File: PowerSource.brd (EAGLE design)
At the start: 95 x 72 mm, 11 parts

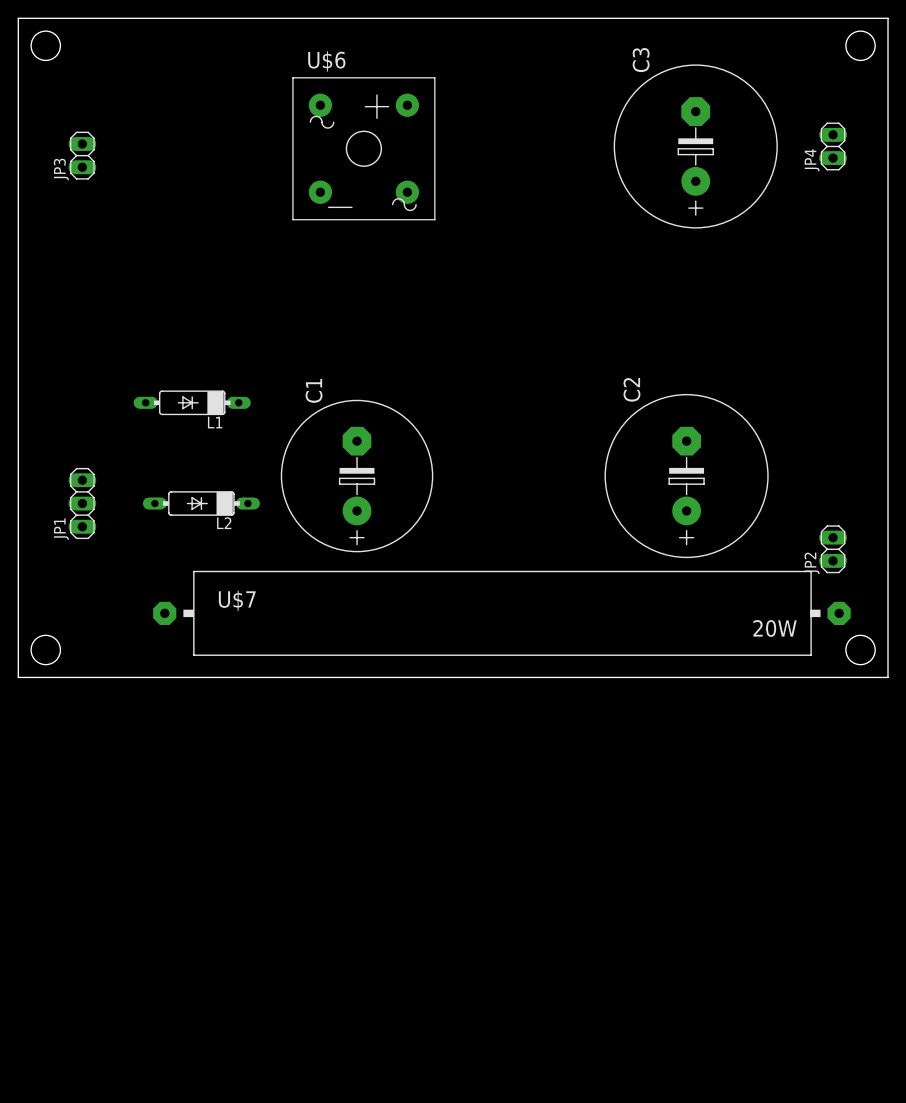
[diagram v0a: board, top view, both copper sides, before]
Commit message: [fix]電源回路を手直し
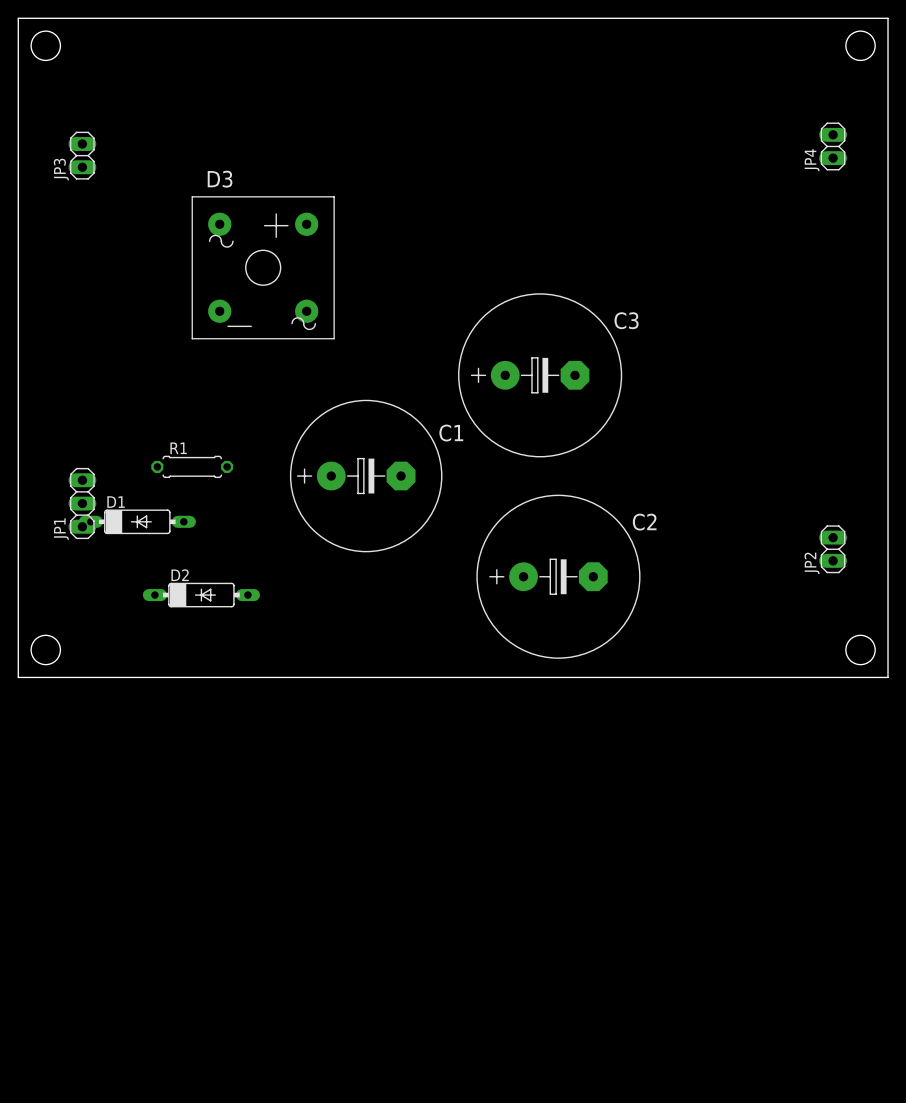
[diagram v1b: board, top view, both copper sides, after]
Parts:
- removed L1, L2: DIODE, VacuumTube:DO07
- removed U$6: BRIDGERECTIFIER, VacuumTube:BRIDGERECTIFIER
- removed U$7: RESISTOR, VacuumTube:RESISTOR
- added D1, D2: (no value), VacuumTube:DO07
- added D3: (no value), VacuumTube:BRIDGERECTIFIER
- added R1: (no value), VacuumTube:0207/7
- C1: value E7.5-16 -> 47u
- C2: value E7.5-18 -> 100u
- C3: value E7.5-18 -> 8800u
- moved C3 30.2 mm to (57.0, 33.0), turned to 0 degrees
- moved C2 17.8 mm to (59.0, 11.0), turned to 0 degrees
- moved C1 1.00 mm to (38.0, 22.0), turned to 0 degrees
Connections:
- net GND: now also D3.AC2; no longer U$6.AC2
- net N$1: now also D2.A; no longer L2.A
- net N$14: now also R1.2; no longer U$7.2
- net N$15: now also D1.C, D2.C, R1.1; no longer L1.C, L2.C, U$7.1
- net N$2: now also D1.A; no longer L1.A
- net N$3: now also D3.-; no longer U$6.-
- net N$4: now also D3.+; no longer U$6.+
- net N$7: now also D3.AC1; no longer U$6.AC1

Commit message: [fix]電源の重大な欠陥
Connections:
- net GND: now also D3.-; no longer D3.AC2
- net N$3: now also D3.AC1; no longer D3.-
- net N$4: now also D3.AC2; no longer D3.+
- net N$7: now also D3.+; no longer D3.AC1
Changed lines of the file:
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@@
 <contactref element="JP2" pad="2"/>
 <contactref element="JP4" pad="2"/>
-<contactref element="D3" pad="AC2"/>
 <contactref element="C1" pad="-"/>
 <contactref element="C2" pad="-"/>
 <contactref element="C3" pad="-"/>
-<wire x1="89" y1="15.27" x2="89" y2="59.27" width="0" layer="19" extent="1-1"/>
-<wire x1="7" y1="16.46" x2="89" y2="15.27" width="0" layer="19" extent="1-1"/>
-<wire x1="31.5" y1="40" x2="7" y2="16.46" width="0" layer="19" extent="1-1"/>
-<wire x1="41.81" y1="22" x2="31.5" y2="40" width="0" layer="19" extent="1-1"/>
-<wire x1="62.81" y1="11" x2="41.81" y2="22" width="0" layer="19" extent="1-1"/>
-<wire x1="60.81" y1="33" x2="62.81" y2="11" width="0" layer="19" extent="1-1"/>
+<contactref element="D3" pad="-"/>
+<wire x1="60.81" y1="33" x2="89" y2="59.27" width="0" layer="19" extent="1-1"/>
+<wire x1="41.81" y1="22" x2="60.81" y2="33" width="0" layer="19" extent="1-1"/>
+<wire x1="62.81" y1="11" x2="60.81" y2="33" width="0" layer="19" extent="1-1"/>
+<wire x1="89" y1="15.27" x2="62.81" y2="11" width="0" layer="19" extent="1-1"/>
+<wire x1="22" y1="40" x2="41.81" y2="22" width="0" layer="19" extent="1-1"/>
+<wire x1="7" y1="16.46" x2="22" y2="40" width="0" layer="19" extent="1-1"/>
 </signal>
 <signal name="N$14">
@@
 <signal name="N$7">
 <contactref element="JP4" pad="1"/>
-<contactref element="D3" pad="AC1"/>
 <contactref element="C3" pad="+"/>
-<wire x1="22" y1="49.5" x2="89" y2="56.73" width="0" layer="19" extent="1-1"/>
-<wire x1="53.19" y1="33" x2="22" y2="49.5" width="0" layer="19" extent="1-1"/>
+<contactref element="D3" pad="+"/>
+<wire x1="53.19" y1="33" x2="89" y2="56.73" width="0" layer="19" extent="1-1"/>
+<wire x1="31.5" y1="49.5" x2="53.19" y2="33" width="0" layer="19" extent="1-1"/>
 </signal>
 <signal name="N$1">
@@
 <wire x1="18.08" y1="17" x2="7" y2="21.54" width="0" layer="19" extent="1-1"/>
 </signal>
-<signal name="N$4">
-<contactref element="JP3" pad="1"/>
-<contactref element="D3" pad="+"/>
-<wire x1="31.5" y1="49.5" x2="7" y2="55.73" width="0" layer="19" extent="1-1"/>
-</signal>
 <signal name="N$3">
 <contactref element="JP3" pad="2"/>
-<contactref element="D3" pad="-"/>
-<wire x1="22" y1="40" x2="7" y2="58.27" width="0" layer="19" extent="1-1"/>
+<contactref element="D3" pad="AC1"/>
+<wire x1="7" y1="58.27" x2="22" y2="49.5" width="0" layer="19" extent="1-1"/>
+</signal>
+<signal name="N$4">
+<contactref element="D3" pad="AC2"/>
+<contactref element="JP3" pad="1"/>
+<wire x1="7" y1="55.73" x2="31.5" y2="40" width="0" layer="19" extent="1-1"/>
 </signal>
 </signals>

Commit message: [fix]電源の直し
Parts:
- C1: value 47u -> 100u
- C2: value 100u -> 47u
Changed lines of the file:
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@@
 <attribute name="VALUE" x="23.555" y="39.92" size="1.778" layer="27" ratio="10"/>
 </element>
-<element name="C1" library="VacuumTube" library_urn="urn:adsk.eagle:library:8044196" package="E7,5-16" package3d_urn="urn:adsk.eagle:package:8399792/3" value="47u" x="38" y="22" smashed="yes">
+<element name="C1" library="VacuumTube" library_urn="urn:adsk.eagle:library:8044196" package="E7,5-16" package3d_urn="urn:adsk.eagle:package:8399792/3" value="100u" x="38" y="22" smashed="yes">
 <attribute name="NAME" x="45.874" y="25.81" size="1.778" layer="25" ratio="10"/>
 <attribute name="VALUE" x="32.92" y="17.7074" size="1.778" layer="27" ratio="10"/>
 </element>
-<element name="C2" library="VacuumTube" library_urn="urn:adsk.eagle:library:8044196" package="E7,5-18" package3d_urn="urn:adsk.eagle:package:8399793/3" value="100u" x="59" y="11" smashed="yes">
+<element name="C2" library="VacuumTube" library_urn="urn:adsk.eagle:library:8044196" package="E7,5-18" package3d_urn="urn:adsk.eagle:package:8399793/3" value="47u" x="59" y="11" smashed="yes">
 <attribute name="NAME" x="67.001" y="16.08" size="1.778" layer="25" ratio="10"/>
 <attribute name="VALUE" x="53.92" y="6.7074" size="1.778" layer="27" ratio="10"/>

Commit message: [add]powerのpdfを作成
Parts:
- C1: value 100u -> 47u
- C2: value 47u -> 100u
- R1: value (none) -> 1k
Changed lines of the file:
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@@
 <attribute name="VALUE" x="23.555" y="39.92" size="1.778" layer="27" ratio="10"/>
 </element>
-<element name="C1" library="VacuumTube" library_urn="urn:adsk.eagle:library:8044196" package="E7,5-16" package3d_urn="urn:adsk.eagle:package:8399792/3" value="100u" x="38" y="22" smashed="yes">
+<element name="C1" library="VacuumTube" library_urn="urn:adsk.eagle:library:8044196" package="E7,5-16" package3d_urn="urn:adsk.eagle:package:8399792/3" value="47u" x="38" y="22" smashed="yes">
 <attribute name="NAME" x="45.874" y="25.81" size="1.778" layer="25" ratio="10"/>
 <attribute name="VALUE" x="32.92" y="17.7074" size="1.778" layer="27" ratio="10"/>
 </element>
-<element name="C2" library="VacuumTube" library_urn="urn:adsk.eagle:library:8044196" package="E7,5-18" package3d_urn="urn:adsk.eagle:package:8399793/3" value="47u" x="59" y="11" smashed="yes">
+<element name="C2" library="VacuumTube" library_urn="urn:adsk.eagle:library:8044196" package="E7,5-18" package3d_urn="urn:adsk.eagle:package:8399793/3" value="100u" x="59" y="11" smashed="yes">
 <attribute name="NAME" x="67.001" y="16.08" size="1.778" layer="25" ratio="10"/>
 <attribute name="VALUE" x="53.92" y="6.7074" size="1.778" layer="27" ratio="10"/>
@@
 <attribute name="VALUE" x="51.92" y="28.7074" size="1.778" layer="27" ratio="10"/>
 </element>
-<element name="R1" library="VacuumTube" library_urn="urn:adsk.eagle:library:8044196" package="0207/7" package3d_urn="urn:adsk.eagle:package:8969348/1" value="" x="19" y="23" smashed="yes">
+<element name="R1" library="VacuumTube" library_urn="urn:adsk.eagle:library:8044196" package="0207/7" package3d_urn="urn:adsk.eagle:package:8969348/1" value="1k" x="19" y="23" smashed="yes">
 <attribute name="NAME" x="16.46" y="24.397" size="1.27" layer="25" ratio="10"/>
 <attribute name="VALUE" x="16.714" y="22.4412" size="1.27" layer="27" ratio="10"/>

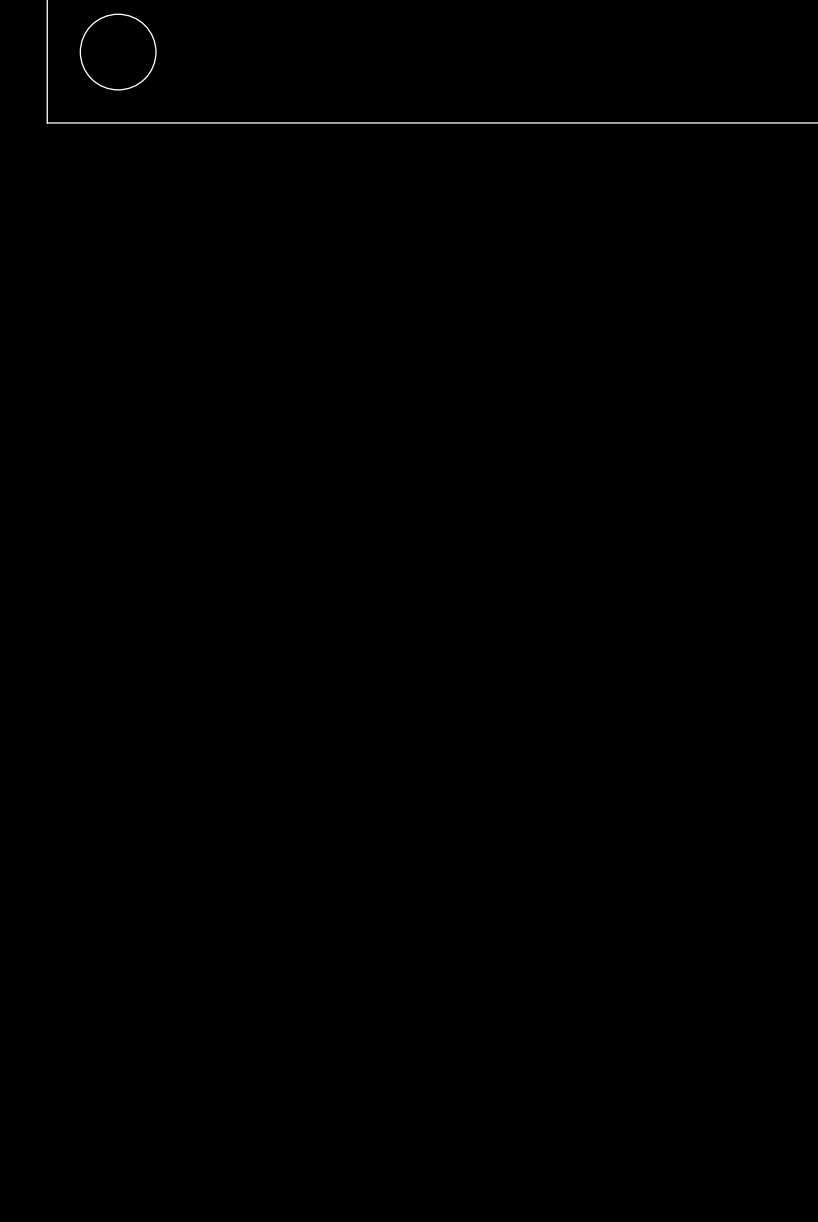
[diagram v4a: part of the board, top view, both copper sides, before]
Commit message: [fix]ヒーター電源を二つ使うことにした
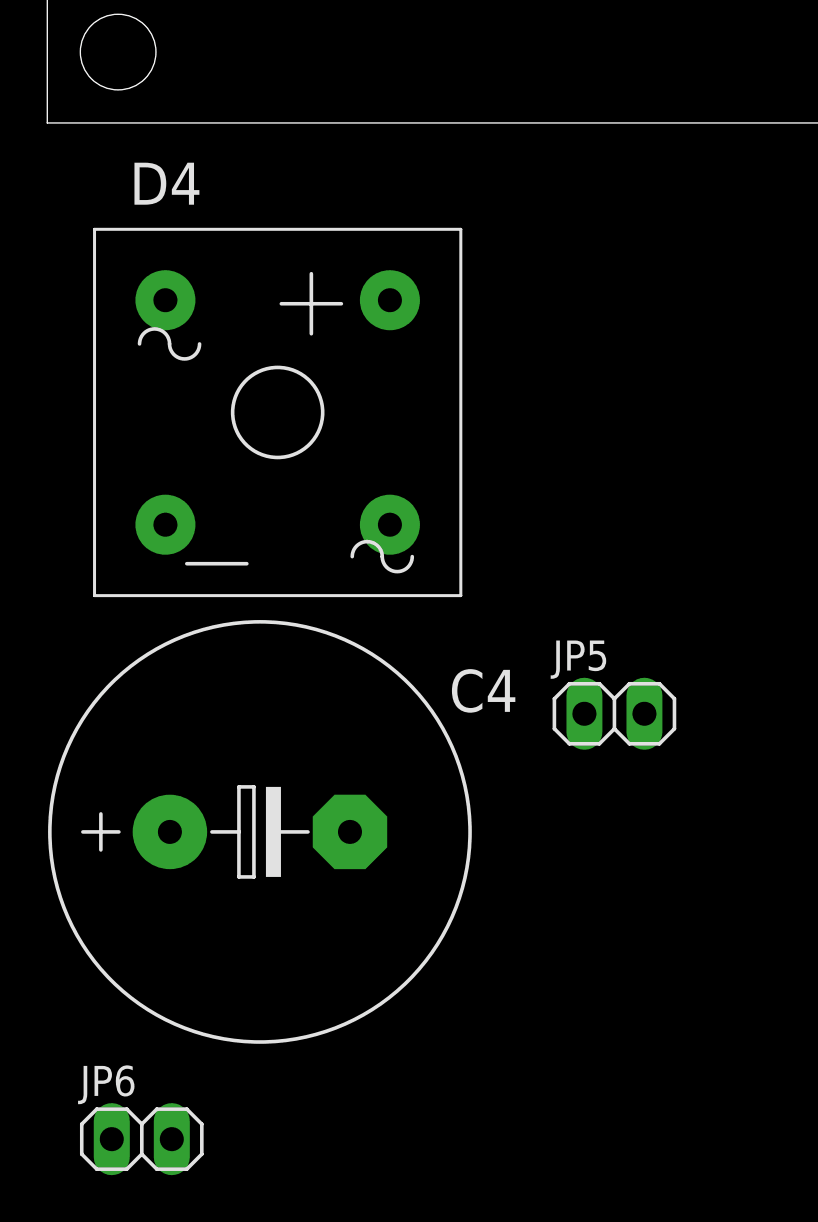
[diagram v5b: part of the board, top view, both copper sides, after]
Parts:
- added C4: 8800u, VacuumTube:E7,5-18
- added D4: (no value), VacuumTube:BRIDGERECTIFIER
- added JP5, JP6: (no value), VacuumTube:1X02
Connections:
- new net N$5: C4.+, D4.+, JP6.1
- new net N$6: D4.AC1, JP5.2
- new net N$8: D4.AC2, JP5.1
- net GND: now also C4.-, D4.-, JP6.2
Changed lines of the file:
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@@
 <attribute name="VALUE" x="16.714" y="22.4412" size="1.27" layer="27" ratio="10"/>
+</element>
+<element name="JP5" library="VacuumTube" library_urn="urn:adsk.eagle:library:8044196" package="1X02" package3d_urn="urn:adsk.eagle:package:22435/2" value="" x="24" y="-25" smashed="yes">
+<attribute name="NAME" x="21.3838" y="-23.1712" size="1.27" layer="25" ratio="10"/>
+<attribute name="VALUE" x="21.46" y="-28.175" size="1.27" layer="27"/>
+</element>
+<element name="JP6" library="VacuumTube" library_urn="urn:adsk.eagle:library:8044196" package="1X02" package3d_urn="urn:adsk.eagle:package:22435/2" value="" x="4" y="-43" smashed="yes">
+<attribute name="NAME" x="1.3838" y="-41.1712" size="1.27" layer="25" ratio="10"/>
+<attribute name="VALUE" x="1.46" y="-46.175" size="1.27" layer="27"/>
+</element>
+<element name="D4" library="VacuumTube" library_urn="urn:adsk.eagle:library:8044196" package="BRIDGERECTIFIER" package3d_urn="urn:adsk.eagle:package:8399794/1" value="" x="2" y="-20" smashed="yes">
+<attribute name="NAME" x="3.475" y="-3.459" size="1.778" layer="25" ratio="10"/>
+<attribute name="VALUE" x="6.555" y="-17.08" size="1.778" layer="27" ratio="10"/>
+</element>
+<element name="C4" library="VacuumTube" library_urn="urn:adsk.eagle:library:8044196" package="E7,5-18" package3d_urn="urn:adsk.eagle:package:8399793/3" value="8800u" x="9" y="-30" smashed="yes">
+<attribute name="NAME" x="17.001" y="-24.92" size="1.778" layer="25" ratio="10"/>
+<attribute name="VALUE" x="3.92" y="-34.2926" size="1.778" layer="27" ratio="10"/>
 </element>
 </elements>
@@
 <contactref element="C3" pad="-"/>
 <contactref element="D3" pad="-"/>
+<contactref element="JP6" pad="2"/>
+<contactref element="C4" pad="-"/>
+<contactref element="D4" pad="-"/>
 <wire x1="60.81" y1="33" x2="89" y2="59.27" width="0" layer="19" extent="1-1"/>
 <wire x1="41.81" y1="22" x2="60.81" y2="33" width="0" layer="19" extent="1-1"/>
@@
 <wire x1="22" y1="40" x2="41.81" y2="22" width="0" layer="19" extent="1-1"/>
 <wire x1="7" y1="16.46" x2="22" y2="40" width="0" layer="19" extent="1-1"/>
+<wire x1="5" y1="-17" x2="7" y2="16.46" width="0" layer="19" extent="1-1"/>
+<wire x1="12.81" y1="-30" x2="5" y2="-17" width="0" layer="19" extent="1-1"/>
+<wire x1="5.27" y1="-43" x2="12.81" y2="-30" width="0" layer="19" extent="1-1"/>
 </signal>
 <signal name="N$14">
@@
 <wire x1="7" y1="55.73" x2="31.5" y2="40" width="0" layer="19" extent="1-1"/>
 </signal>
+<signal name="N$5">
+<contactref element="JP6" pad="1"/>
+<contactref element="C4" pad="+"/>
+<contactref element="D4" pad="+"/>
+<wire x1="5.19" y1="-30" x2="2.73" y2="-43" width="0" layer="19" extent="1-1"/>
+<wire x1="14.5" y1="-7.5" x2="5.19" y2="-30" width="0" layer="19" extent="1-1"/>
+</signal>
+<signal name="N$6">
+<contactref element="JP5" pad="2"/>
+<contactref element="D4" pad="AC1"/>
+<wire x1="25.27" y1="-25" x2="5" y2="-7.5" width="0" layer="19" extent="1-1"/>
+</signal>
+<signal name="N$8">
+<contactref element="D4" pad="AC2"/>
+<contactref element="JP5" pad="1"/>
+<wire x1="22.73" y1="-25" x2="14.5" y2="-17" width="0" layer="19" extent="1-1"/>
+</signal>
 </signals>
